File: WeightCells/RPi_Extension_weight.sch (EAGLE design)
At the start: 32 parts, among them U1 AD7730BRUZ, U2 AD7730BRUZ, U3 AD7730BRUZ, U4 AD7730BRUZ, U5 AD7730BRUZ, U6 AD7730BRUZ, U7 AD7730BRUZ, U8 AD7730BRUZ, U9 STM32F103RCT6

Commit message: vias revisited
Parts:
- C2, C3, C4, C5, C6: value (none) -> 100nf
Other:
- moved on the sheet: C3, C4, C5, C6
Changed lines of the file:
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@@
 <part name="GND1" library="supply1" deviceset="GND" device=""/>
 <part name="GND6" library="supply1" deviceset="GND" device=""/>
-<part name="C2" library="rcl" deviceset="C-EU" device="C0603"/>
-<part name="C3" library="rcl" deviceset="C-EU" device="C0603"/>
-<part name="C4" library="rcl" deviceset="C-EU" device="C0603"/>
-<part name="C5" library="rcl" deviceset="C-EU" device="C0603"/>
-<part name="C6" library="rcl" deviceset="C-EU" device="C0603"/>
+<part name="C2" library="rcl" deviceset="C-EU" device="C0603" value="100nf"/>
+<part name="C3" library="rcl" deviceset="C-EU" device="C0603" value="100nf"/>
+<part name="C4" library="rcl" deviceset="C-EU" device="C0603" value="100nf"/>
+<part name="C5" library="rcl" deviceset="C-EU" device="C0603" value="100nf"/>
+<part name="C6" library="rcl" deviceset="C-EU" device="C0603" value="100nf"/>
 <part name="GND7" library="supply1" deviceset="GND" device=""/>
 <part name="GND8" library="supply1" deviceset="GND" device=""/>
@@
 <instance part="GND6" gate="1" x="144.78" y="-104.14"/>
 <instance part="C2" gate="G$1" x="134.62" y="25.4"/>
-<instance part="C3" gate="G$1" x="124.46" y="10.16"/>
-<instance part="C4" gate="G$1" x="129.54" y="10.16"/>
-<instance part="C5" gate="G$1" x="134.62" y="10.16"/>
-<instance part="C6" gate="G$1" x="139.7" y="10.16"/>
+<instance part="C3" gate="G$1" x="106.68" y="10.16"/>
+<instance part="C4" gate="G$1" x="116.84" y="10.16"/>
+<instance part="C5" gate="G$1" x="127" y="10.16"/>
+<instance part="C6" gate="G$1" x="137.16" y="10.16"/>
 <instance part="GND7" gate="1" x="134.62" y="33.02" rot="MR180"/>
-<instance part="GND8" gate="1" x="114.3" y="5.08" rot="MR90"/>
+<instance part="GND8" gate="1" x="101.6" y="2.54" rot="MR0"/>
 <instance part="SV4" gate="1" x="66.04" y="15.24"/>
 <instance part="P+3" gate="1" x="271.78" y="195.58"/>
@@
 <pinref part="C6" gate="G$1" pin="2"/>
 <pinref part="C5" gate="G$1" pin="2"/>
-<wire x1="139.7" y1="5.08" x2="134.62" y2="5.08" width="0.1524" layer="91"/>
+<wire x1="137.16" y1="5.08" x2="127" y2="5.08" width="0.1524" layer="91"/>
 <pinref part="C4" gate="G$1" pin="2"/>
-<wire x1="134.62" y1="5.08" x2="129.54" y2="5.08" width="0.1524" layer="91"/>
-<junction x="134.62" y="5.08"/>
+<wire x1="127" y1="5.08" x2="116.84" y2="5.08" width="0.1524" layer="91"/>
+<junction x="127" y="5.08"/>
 <pinref part="C3" gate="G$1" pin="2"/>
-<wire x1="129.54" y1="5.08" x2="124.46" y2="5.08" width="0.1524" layer="91"/>
-<junction x="129.54" y="5.08"/>
+<wire x1="116.84" y1="5.08" x2="106.68" y2="5.08" width="0.1524" layer="91"/>
+<junction x="116.84" y="5.08"/>
 <pinref part="GND8" gate="1" pin="GND"/>
-<wire x1="124.46" y1="5.08" x2="116.84" y2="5.08" width="0.1524" layer="91"/>
-<junction x="124.46" y="5.08"/>
+<wire x1="106.68" y1="5.08" x2="101.6" y2="5.08" width="0.1524" layer="91"/>
+<junction x="106.68" y="5.08"/>
 </segment>
 <segment>
@@
 <pinref part="U9" gate="A" pin="VDD_1"/>
 <wire x1="144.78" y1="10.16" x2="152.4" y2="10.16" width="0.1524" layer="91"/>
-<wire x1="144.78" y1="12.7" x2="139.7" y2="12.7" width="0.1524" layer="91"/>
-<label x="114.3" y="12.7" size="1.778" layer="95"/>
+<wire x1="144.78" y1="12.7" x2="137.16" y2="12.7" width="0.1524" layer="91"/>
+<label x="96.52" y="12.7" size="1.778" layer="95"/>
 <pinref part="C3" gate="G$1" pin="1"/>
-<wire x1="139.7" y1="12.7" x2="134.62" y2="12.7" width="0.1524" layer="91"/>
-<wire x1="134.62" y1="12.7" x2="129.54" y2="12.7" width="0.1524" layer="91"/>
-<wire x1="129.54" y1="12.7" x2="124.46" y2="12.7" width="0.1524" layer="91"/>
-<wire x1="124.46" y1="12.7" x2="121.92" y2="12.7" width="0.1524" layer="91"/>
-<junction x="124.46" y="12.7"/>
+<wire x1="137.16" y1="12.7" x2="127" y2="12.7" width="0.1524" layer="91"/>
+<wire x1="127" y1="12.7" x2="116.84" y2="12.7" width="0.1524" layer="91"/>
+<wire x1="116.84" y1="12.7" x2="106.68" y2="12.7" width="0.1524" layer="91"/>
+<wire x1="106.68" y1="12.7" x2="104.14" y2="12.7" width="0.1524" layer="91"/>
+<junction x="106.68" y="12.7"/>
 <pinref part="C4" gate="G$1" pin="1"/>
-<junction x="129.54" y="12.7"/>
+<junction x="116.84" y="12.7"/>
 <pinref part="C5" gate="G$1" pin="1"/>
-<junction x="134.62" y="12.7"/>
+<junction x="127" y="12.7"/>
 <pinref part="C6" gate="G$1" pin="1"/>
-<junction x="139.7" y="12.7"/>
+<junction x="137.16" y="12.7"/>
 <wire x1="144.78" y1="10.16" x2="144.78" y2="5.08" width="0.1524" layer="91"/>
 <junction x="144.78" y="10.16"/>

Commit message: updated pcbs
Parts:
- added C10, C9: 0.1uf, rcl:C-EUC0603
- renumbered U$1 to Y2, U$2 to Y1
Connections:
- net DVCC: now also C10.1, C9.1
- net GND: now also C10.2, C9.2
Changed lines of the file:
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@@
 <part name="GND4" library="supply1" deviceset="GND" device=""/>
 <part name="U9" library="STM32F103RCT6" deviceset="STM32F103RCT6" device=""/>
-<part name="U$1" library="kc2520b_c1" deviceset="KC2520B-C1" device=""/>
+<part name="Y2" library="kc2520b_c1" deviceset="KC2520B-C1" device=""/>
 <part name="GND15" library="supply1" deviceset="GND" device=""/>
 <part name="C1" library="rcl" deviceset="C-EU" device="C0603" value="0.1uf"/>
@@
 <part name="GND26" library="supply1" deviceset="GND" device=""/>
 <part name="P+17" library="supply1" deviceset="+5V" device=""/>
-<part name="U$2" library="ABM3B" deviceset="ABM3B" device=""/>
+<part name="Y1" library="ABM3B" deviceset="ABM3B" device=""/>
 <part name="GND27" library="supply1" deviceset="GND" device=""/>
 <part name="GND28" library="supply1" deviceset="GND" device=""/>
 <part name="C7" library="rcl" deviceset="C-EU" device="C0603" value="33pf"/>
 <part name="C8" library="rcl" deviceset="C-EU" device="C0603" value="33pf"/>
+<part name="GND29" library="supply1" deviceset="GND" device=""/>
+<part name="GND30" library="supply1" deviceset="GND" device=""/>
+<part name="C9" library="rcl" deviceset="C-EU" device="C0603" value="0.1uf"/>
+<part name="C10" library="rcl" deviceset="C-EU" device="C0603" value="0.1uf"/>
 </parts>
 <sheets>
@@
 <instance part="GND4" gate="1" x="368.3" y="193.04" rot="R180"/>
 <instance part="U9" gate="A" x="182.88" y="-35.56"/>
-<instance part="U$1" gate="G$1" x="71.12" y="228.6"/>
+<instance part="Y2" gate="G$1" x="71.12" y="228.6"/>
 <instance part="GND15" gate="1" x="50.8" y="223.52" rot="R270"/>
 <instance part="C1" gate="G$1" x="86.36" y="241.3"/>
@@
 <instance part="GND26" gate="1" x="139.7" y="73.66" rot="R270"/>
 <instance part="P+17" gate="1" x="144.78" y="66.04" rot="R180"/>
-<instance part="U$2" gate="G$1" x="266.7" y="15.24"/>
+<instance part="Y1" gate="G$1" x="266.7" y="15.24"/>
 <instance part="GND27" gate="1" x="287.02" y="27.94" rot="MR180"/>
 <instance part="GND28" gate="1" x="248.92" y="5.08" rot="MR0"/>
 <instance part="C7" gate="G$1" x="269.24" y="2.54" rot="R270"/>
 <instance part="C8" gate="G$1" x="266.7" y="27.94" rot="R90"/>
+<instance part="GND29" gate="1" x="673.1" y="157.48"/>
+<instance part="GND30" gate="1" x="673.1" y="78.74"/>
+<instance part="C9" gate="G$1" x="673.1" y="88.9"/>
+<instance part="C10" gate="G$1" x="673.1" y="167.64"/>
 </instances>
 <busses>
@@
 </segment>
 <segment>
-<pinref part="U$1" gate="G$1" pin="GND"/>
+<pinref part="Y2" gate="G$1" pin="GND"/>
 <pinref part="GND15" gate="1" pin="GND"/>
 <wire x1="58.42" y1="223.52" x2="53.34" y2="223.52" width="0.1524" layer="91"/>
@@
 </segment>
 <segment>
-<pinref part="U$2" gate="G$1" pin="GND1"/>
+<pinref part="Y1" gate="G$1" pin="GND1"/>
 <pinref part="GND28" gate="1" pin="GND"/>
 <wire x1="251.46" y1="10.16" x2="248.92" y2="10.16" width="0.1524" layer="91"/>
@@
 </segment>
 <segment>
-<pinref part="U$2" gate="G$1" pin="GND2"/>
+<pinref part="Y1" gate="G$1" pin="GND2"/>
 <wire x1="281.94" y1="22.86" x2="287.02" y2="22.86" width="0.1524" layer="91"/>
 <pinref part="GND27" gate="1" pin="GND"/>
@@
 <wire x1="281.94" y1="27.94" x2="281.94" y2="22.86" width="0.1524" layer="91"/>
 <junction x="281.94" y="22.86"/>
+</segment>
+<segment>
+<pinref part="GND30" gate="1" pin="GND"/>
+<pinref part="C9" gate="G$1" pin="2"/>
+<wire x1="673.1" y1="81.28" x2="673.1" y2="83.82" width="0.1524" layer="91"/>
+</segment>
+<segment>
+<pinref part="GND29" gate="1" pin="GND"/>
+<pinref part="C10" gate="G$1" pin="2"/>
+<wire x1="673.1" y1="160.02" x2="673.1" y2="162.56" width="0.1524" layer="91"/>
 </segment>
 </net>
@@
 </segment>
 <segment>
-<pinref part="U$1" gate="G$1" pin="VCC"/>
+<pinref part="Y2" gate="G$1" pin="VCC"/>
 <wire x1="83.82" y1="233.68" x2="86.36" y2="233.68" width="0.1524" layer="91"/>
 <label x="91.44" y="233.68" size="1.778" layer="95"/>
@@
 <label x="238.76" y="78.74" size="1.778" layer="95"/>
 </segment>
+<segment>
+<pinref part="C10" gate="G$1" pin="1"/>
+<wire x1="673.1" y1="170.18" x2="673.1" y2="175.26" width="0.1524" layer="91"/>
+<label x="673.1" y="175.26" size="1.778" layer="95"/>
+</segment>
+<segment>
+<pinref part="C9" gate="G$1" pin="1"/>
+<wire x1="673.1" y1="91.44" x2="673.1" y2="96.52" width="0.1524" layer="91"/>
+<label x="673.1" y="96.52" size="1.778" layer="95"/>
+</segment>
 </net>
 <net name="MOSI" class="0">
@@
 <net name="MCLK" class="0">
 <segment>
-<pinref part="U$1" gate="G$1" pin="OUT"/>
+<pinref part="Y2" gate="G$1" pin="OUT"/>
 <wire x1="83.82" y1="223.52" x2="91.44" y2="223.52" width="0.1524" layer="91"/>
 <label x="91.44" y="223.52" size="1.778" layer="95"/>
@@
 <net name="N$2" class="0">
 <segment>
-<pinref part="U$2" gate="G$1" pin="OSC1"/>
+<pinref part="Y1" gate="G$1" pin="OSC1"/>
 <wire x1="251.46" y1="22.86" x2="243.84" y2="22.86" width="0.1524" layer="91"/>
 <wire x1="243.84" y1="22.86" x2="243.84" y2="15.24" width="0.1524" layer="91"/>
@@
 <net name="N$3" class="0">
 <segment>
-<pinref part="U$2" gate="G$1" pin="OSC2"/>
+<pinref part="Y1" gate="G$1" pin="OSC2"/>
 <wire x1="281.94" y1="10.16" x2="287.02" y2="10.16" width="0.1524" layer="91"/>
 <wire x1="287.02" y1="10.16" x2="287.02" y2="-2.54" width="0.1524" layer="91"/>

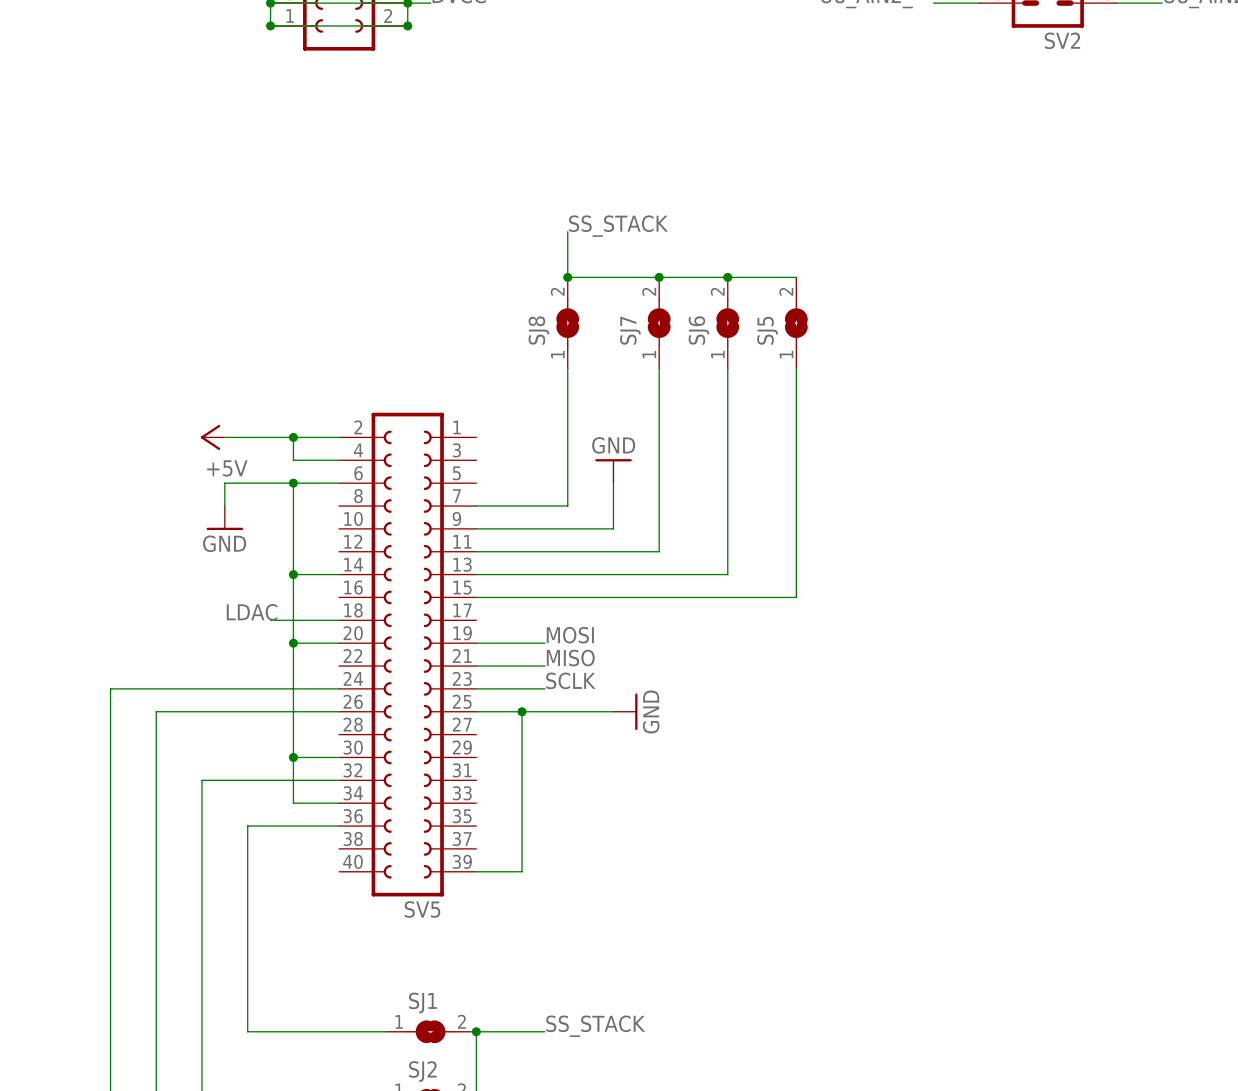
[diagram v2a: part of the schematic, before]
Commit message: added address lines up to 16 to loadcell board
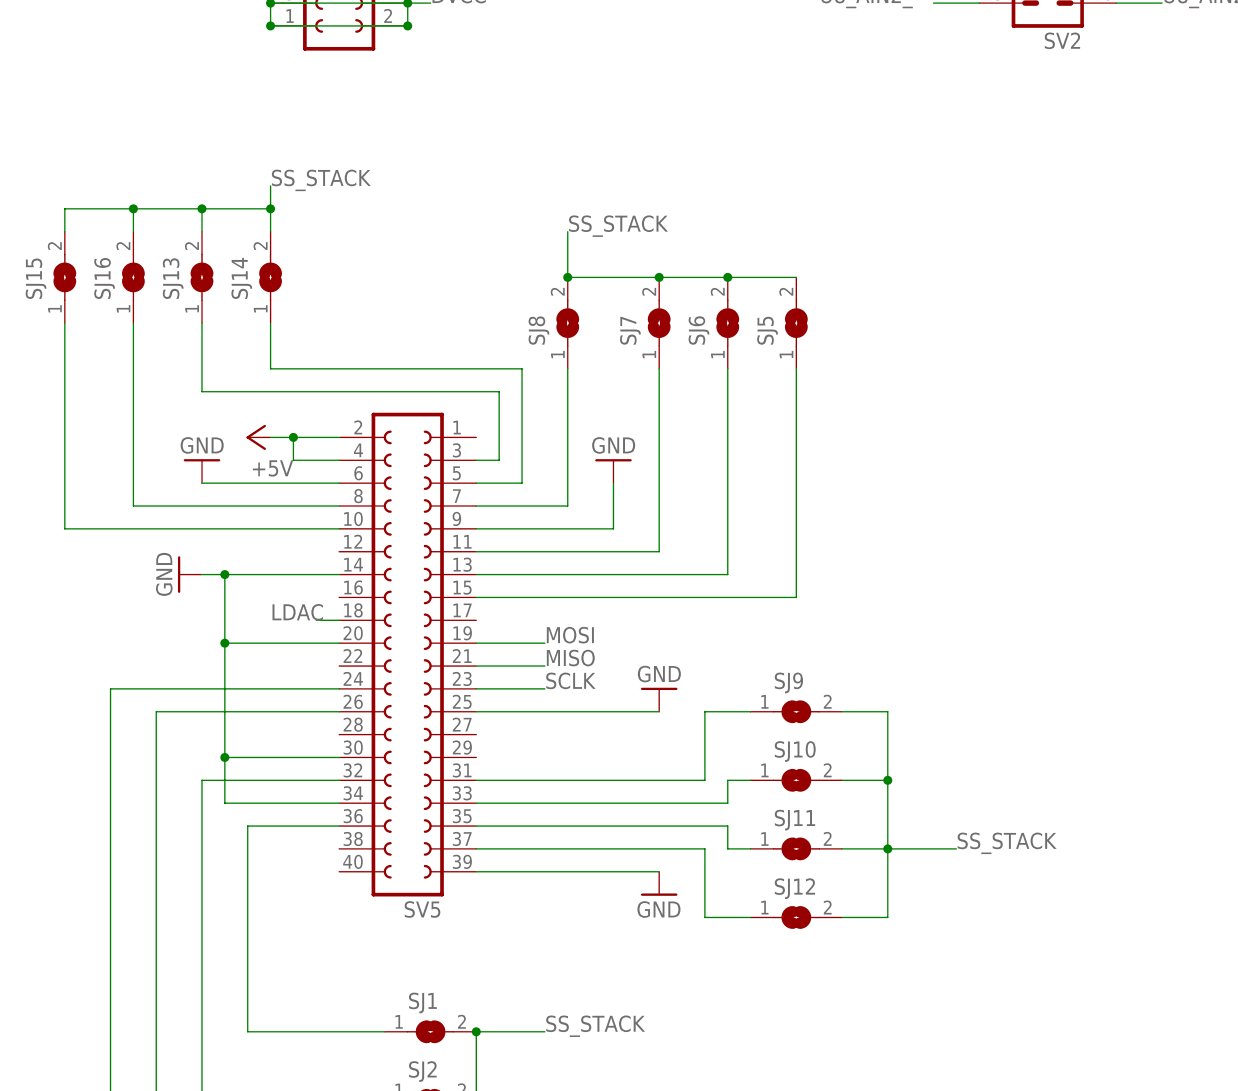
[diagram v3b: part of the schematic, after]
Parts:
- added SJ10, SJ11, SJ12, SJ13, SJ14, SJ15, SJ16, SJ9: (no value), jumper:SJ
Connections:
- new net N$1: SJ12.1, SV5.37
- new net N$10: SJ14.1, SV5.5
- new net N$4: SJ11.1, SV5.35
- new net N$5: SJ10.1, SV5.33
- new net N$6: SJ9.1, SV5.31
- new net N$7: SJ16.1, SV5.8
- new net N$8: SJ15.1, SV5.10
- new net N$9: SJ13.1, SV5.3
- net SS_STACK: now also SJ10.2, SJ11.2, SJ12.2, SJ13.2, SJ14.2, SJ15.2, SJ16.2, SJ9.2
